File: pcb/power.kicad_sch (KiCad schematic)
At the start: 27 parts, among them U16 AP22811AW5-7‎, U17 MT3410LB, U18 LP5907MFX-3.3, U4 MT3410LB

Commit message: hub reset handled by DC-DC power good switch to TLV62585P DC-DC for power good remove reset button - can just plug cable add buttons to ground SDA, SCL as hub bypass to allow programming
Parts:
- removed U17, U4: MT3410LB, kicad_pcb:SOT-23-5, symbol launch:MT3410LB
- added U17, U4: TLV62585DRLR, launch:SOT-563, symbol launch:TLV62585DRLR
- C32, C34, C35, C48, C49, C50: value 22 uF -> 10 uF
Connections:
- net FB1V1: now also U4.5 (FB)
- net FB3V6: now also U17.5 (FB)
- net GND: now also U17.1 (GND), U4.1 (GND)
- net SW1V1: now also U4.2 (SW)
- net SW3V6: now also U17.2 (SW)
- net VCC: now also U17.3 (VIN), U17.4 (EN), U4.3 (VIN), U4.4 (EN)
- new net PG: U17.6 (PG), U4.6 (PG)

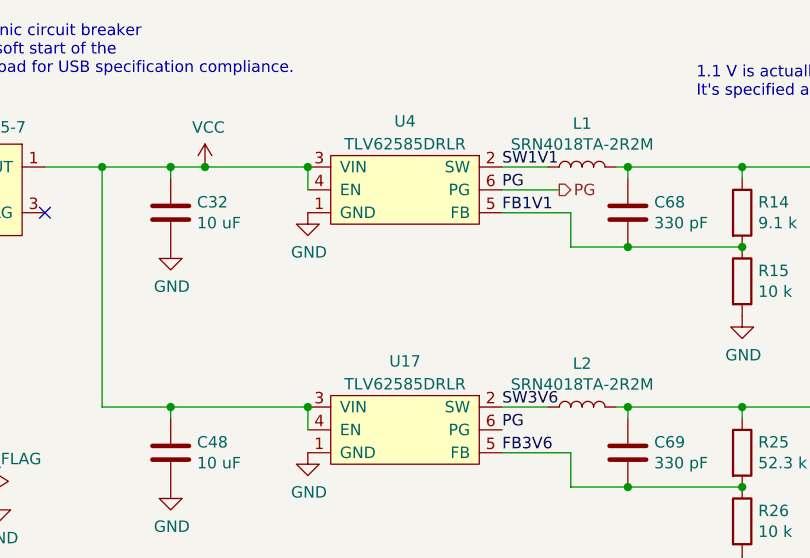
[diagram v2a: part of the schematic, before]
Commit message: BOM update USB7206CT/KDX, TLV62585PDRLR
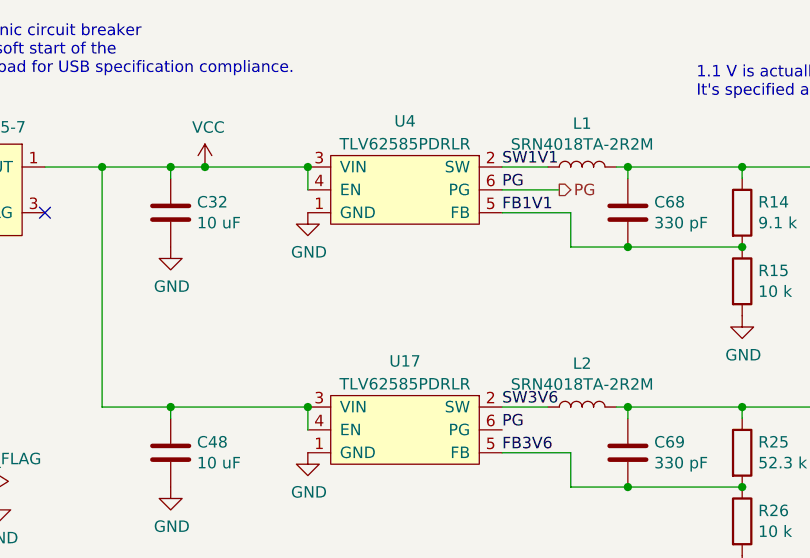
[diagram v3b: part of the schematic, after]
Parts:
- U17, U4: value TLV62585DRLR -> TLV62585PDRLR
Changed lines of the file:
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@@
       (effects (font (size 1.27 1.27)))
     )
-    (property "Value" "TLV62585DRLR" (at 126.365 106.68 0)
+    (property "Value" "TLV62585PDRLR" (at 126.365 106.68 0)
       (effects (font (size 1.27 1.27)))
     )
@@
       (effects (font (size 1.27 1.27)))
     )
-    (property "Value" "TLV62585DRLR" (at 126.365 133.35 0)
+    (property "Value" "TLV62585PDRLR" (at 126.365 133.35 0)
       (effects (font (size 1.27 1.27)))
     )

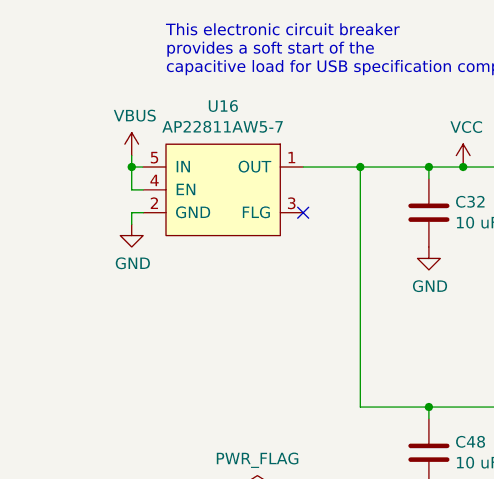
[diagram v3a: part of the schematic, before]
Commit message: VBUS protection circuitry add capacitors at every USB power switch add reverse protection schottky diode     to clamp observed negative voltages seen on VBUS during plug and unplug add RC snubber to VBUS
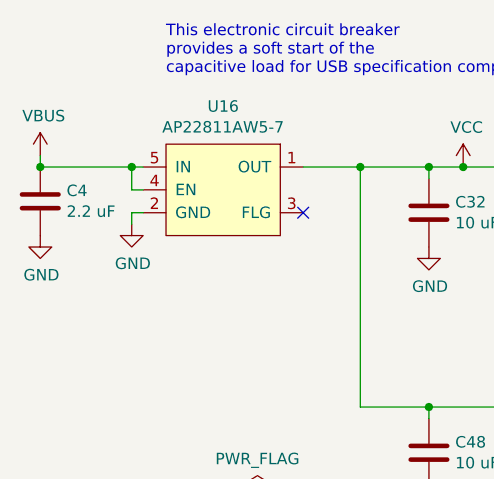
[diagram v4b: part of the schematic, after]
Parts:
- added C4: 2.2 uF, Capacitor_SMD:C_0603_1608Metric, symbol Device:C
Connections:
- net GND: now also C4.2
- net VBUS: now also C4.1
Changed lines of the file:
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@@
     (title "Launch")
     (date "2023-05-08")
-    (rev "3.1")
+    (rev "3.2")
     (company "System76")
   )
@@
   )
   (junction (at 187.96 109.22) (diameter 0) (color 0 0 0 0)
+  )
+  (junction (at 57.15 109.22) (diameter 0) (color 0 0 0 0)
   )
   (junction (at 177.8 109.22) (diameter 0) (color 0 0 0 0)
@@
     (stroke (width 0) (type default))
   )
-  (wire (pts (xy 67.31 109.22) (xy 67.31 107.95))
+  (wire (pts (xy 57.15 109.22) (xy 57.15 107.95))
     (stroke (width 0) (type default))
   )
@@
   )
   (wire (pts (xy 151.13 109.22) (xy 163.83 109.22))
+    (stroke (width 0) (type default))
+  )
+  (wire (pts (xy 57.15 109.22) (xy 67.31 109.22))
     (stroke (width 0) (type default))
   )
@@
     )
   )
-  (symbol (lib_id "power:VBUS") (at 67.31 107.95 0) (unit 1)
-    (in_bom yes) (on_board yes) (dnp no)
-    (property "Reference" "#PWR0252" (at 67.31 111.76 0)
-      (effects (font (size 1.27 1.27)) hide)
-    )
-    (property "Value" "VBUS" (at 67.691 103.5558 0)
-      (effects (font (size 1.27 1.27)))
-    )
-    (property "Footprint" "" (at 67.31 107.95 0)
-      (effects (font (size 1.27 1.27)) hide)
-    )
-    (property "Datasheet" "" (at 67.31 107.95 0)
+  (symbol (lib_id "power:VBUS") (at 57.15 107.95 0) (unit 1)
+    (in_bom yes) (on_board yes) (dnp no)
+    (property "Reference" "#PWR0252" (at 57.15 111.76 0)
+      (effects (font (size 1.27 1.27)) hide)
+    )
+    (property "Value" "VBUS" (at 57.531 103.5558 0)
+      (effects (font (size 1.27 1.27)))
+    )
+    (property "Footprint" "" (at 57.15 107.95 0)
+      (effects (font (size 1.27 1.27)) hide)
+    )
+    (property "Datasheet" "" (at 57.15 107.95 0)
       (effects (font (size 1.27 1.27)) hide)
     )
@@
         (path "/80c969df-cd39-4c4a-8336-5a366308cfd3/00000000-0000-0000-0000-00005f8e2a01"
           (reference "#PWR0374") (unit 1)
+        )
+      )
+    )
+  )
+  (symbol (lib_id "Device:C") (at 57.15 113.03 0) (unit 1)
+    (in_bom yes) (on_board yes) (dnp no)
+    (property "Reference" "C4" (at 60.071 111.8616 0)
+      (effects (font (size 1.27 1.27)) (justify left))
+    )
+    (property "Value" "2.2 uF" (at 60.071 114.173 0)
+      (effects (font (size 1.27 1.27)) (justify left))
+    )
+    (property "Footprint" "Capacitor_SMD:C_0603_1608Metric" (at 58.1152 116.84 0)
+      (effects (font (size 1.27 1.27)) hide)
+    )
+    (property "Datasheet" "~" (at 57.15 113.03 0)
+      (effects (font (size 1.27 1.27)) hide)
+    )
+    (property "Manufacturer" "Generic X5R capacitor" (at 57.15 113.03 0)
+      (effects (font (size 1.27 1.27)) hide)
+    )
+    (pin "1")
+    (pin "2")
+    (instances
+      (project "launch"
+        (path "/80c969df-cd39-4c4a-8336-5a366308cfd3/00000000-0000-0000-0000-00005f8e2a01"
+          (reference "C4") (unit 1)
         )
       )
@@
         )
       )
+    )
+  )
+  (symbol (lib_id "power:GND") (at 57.15 116.84 0) (unit 1)
+    (in_bom yes) (on_board yes) (dnp no)
+    (property "Reference" "#PWR03" (at 57.15 123.19 0)
+      (effects (font (size 1.27 1.27)) hide)
+    )
+    (property "Value" "GND" (at 57.277 121.2342 0)
+      (effects (font (size 1.27 1.27)))
+    )
+    (property "Footprint" "" (at 57.15 116.84 0)
+      (effects (font (size 1.27 1.27)) hide)
+    )
+    (property "Datasheet" "" (at 57.15 116.84 0)
+      (effects (font (size 1.27 1.27)) hide)
+    )
+    (pin "1")
+    (instances
+      (project "launch"
+        (path "/80c969df-cd39-4c4a-8336-5a366308cfd3/00000000-0000-0000-0000-00005f8e2a01"
+          (reference "#PWR03") (unit 1)
+        )
+      )
